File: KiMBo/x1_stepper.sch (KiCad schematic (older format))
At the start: 26 parts

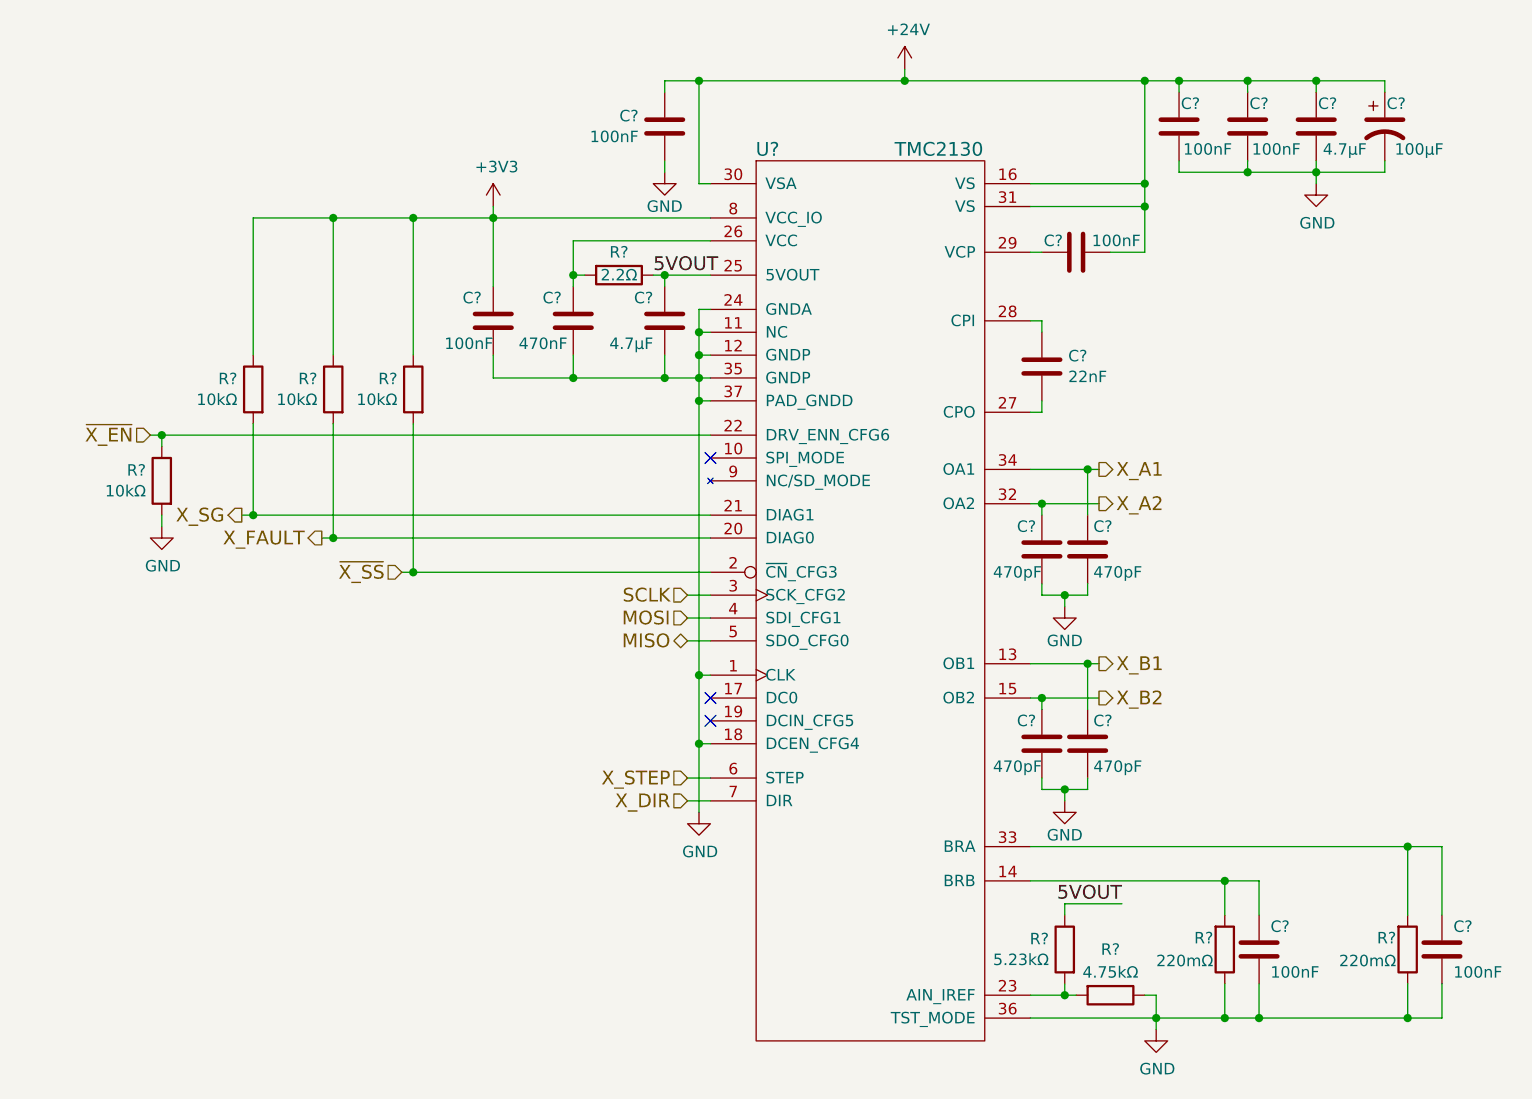
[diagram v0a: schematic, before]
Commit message: Update the rest of the power rails and add two more stepper drivers
Now has *nine* stepper drivers, this will increase cost, and may drastically increase development time...
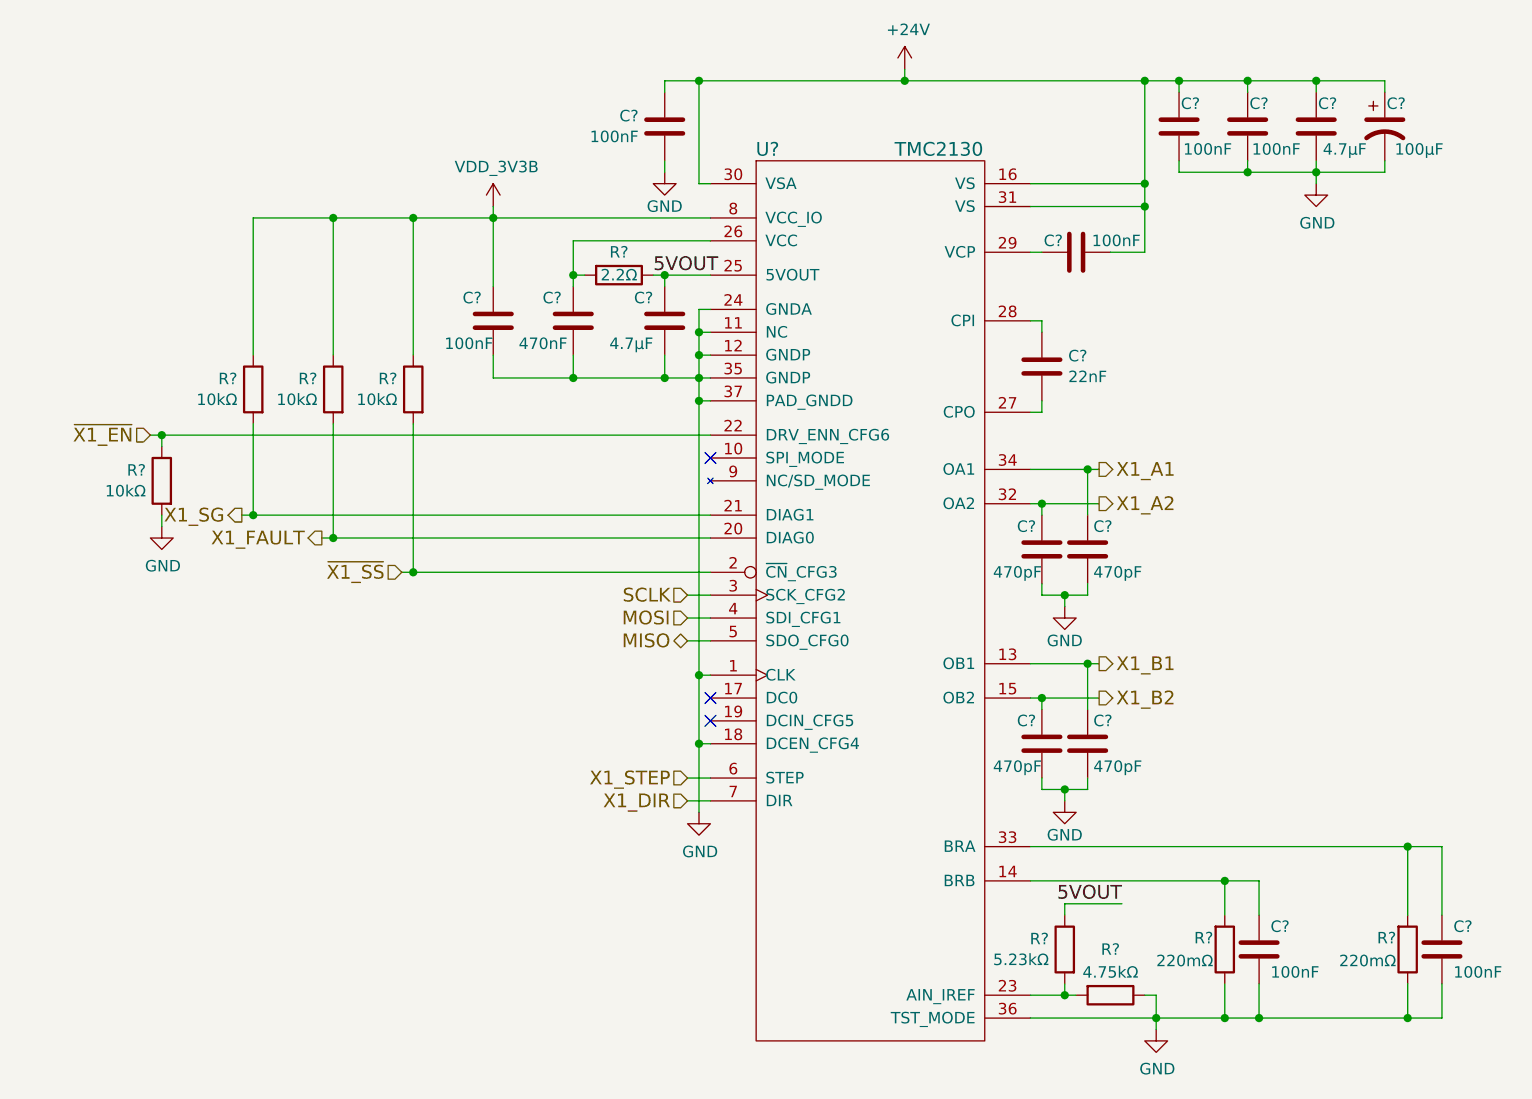
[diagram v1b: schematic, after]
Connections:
- net +3V3 renamed VDD_3V3B
- net X_A1 renamed X1_A1
- net X_A2 renamed X1_A2
- net X_B1 renamed X1_B1
- net X_B2 renamed X1_B2
- net X_DIR renamed X1_DIR
- net X_FAULT renamed X1_FAULT
- net X_SG renamed X1_SG
- net X_STEP renamed X1_STEP
- net ~X_EN renamed ~X1_EN
- net ~X_SS renamed ~X1_SS
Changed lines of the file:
@@
 $Descr A3 16535 11693
 encoding utf-8
-Sheet 13 25
+Sheet 27 27
 Title ""
 Date ""
@@
 $EndDescr
 Text HLabel 9400 4600 2    60   Output ~ 0
-X_A1
+X1_A1
 Text HLabel 9400 4750 2    60   Output ~ 0
-X_A2
+X1_A2
 Text HLabel 9400 5450 2    60   Output ~ 0
-X_B1
+X1_B1
 Text HLabel 9400 5600 2    60   Output ~ 0
-X_B2
+X1_B2
 Text HLabel 7600 5950 0    60   Input ~ 0
-X_STEP
+X1_STEP
 Text HLabel 7600 6050 0    60   Input ~ 0
-X_DIR
+X1_DIR
 Text HLabel 6350 5050 0    60   Input ~ 0
-~X_SS
+~X1_SS
 Text HLabel 7600 5150 0    60   Input ~ 0
 SCLK
@@
 MOSI
 Text HLabel 5650 4800 0    60   Output ~ 0
-X_SG
+X1_SG
 $Comp
 L C C?
@@
 	-1   0    0    -1
 $EndComp
-$Comp
-L +3V3 #PWR?
-U 1 1 58C0931C
-P 6750 3450
-F 0 "#PWR?" H 6750 3300 50  0001 C CNN
-F 1 "+3V3" H 6765 3623 50  0000 C CNN
-F 2 "" H 6750 3450 50  0000 C CNN
-F 3 "" H 6750 3450 50  0000 C CNN
-	1    6750 3450
-	1    0    0    -1
-$EndComp
 NoConn ~ 7700 5700
 $Comp
@@
 $EndComp
 Text HLabel 6000 4900 0    60   Output ~ 0
-X_FAULT
+X1_FAULT
 $Comp
 L R R?
@@
 $EndComp
 Text HLabel 5250 4450 0    60   Input ~ 0
-~X_EN
+~X1_EN
 NoConn ~ 7700 4550
 $Comp
@@
 Wire Wire Line
 	5300 4450 5300 4500
+$Comp
+L VDD_3V3B #PWR?
+U 1 1 5A2FF856
+P 6750 3450
+F 0 "#PWR?" H 6750 3300 50  0001 C CNN
+F 1 "VDD_3V3B" H 6765 3623 50  0000 C CNN
+F 2 "" H 6750 3450 50  0000 C CNN
+F 3 "" H 6750 3450 50  0000 C CNN
+	1    6750 3450
+	1    0    0    -1
+$EndComp
 $EndSCHEMATC

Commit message: Use only one driver on Y, NAND X and Z FAULT and SG signals
Dual X carriage will need to be tested to determine if two seperate drivers are required for X
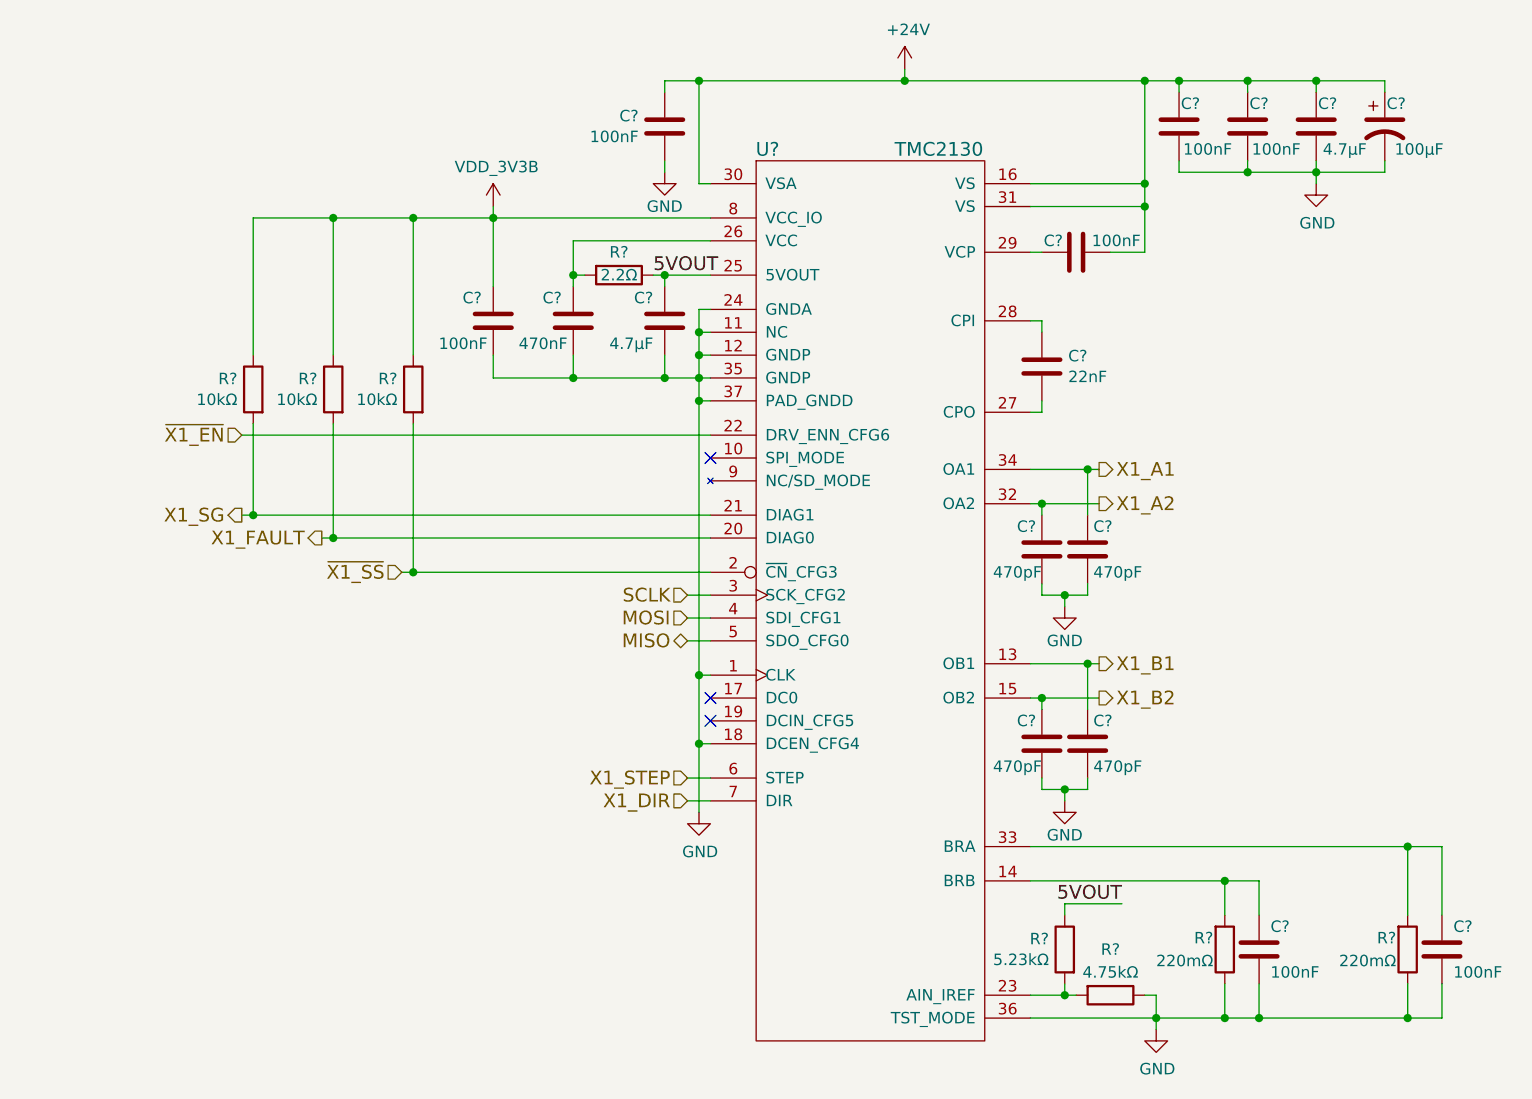
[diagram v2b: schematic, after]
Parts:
- removed C?: 100nF, symbol C
- removed R?: 10kΩ, symbol R
- added C?: 100nF, symbol C
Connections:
- net GND: now also C?.2
- net VDD_3V3B: now also C?.1
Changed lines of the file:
@@
 $Descr A3 16535 11693
 encoding utf-8
-Sheet 27 27
+Sheet 27 26
 Title ""
 Date ""
@@
 	-1   0    0    -1
 $EndComp
-$Comp
-L C C?
-U 1 1 58C09315
-P 6750 3950
-F 0 "C?" H 6800 4050 50  0000 L CNN
-F 1 "100nF" H 6750 3850 50  0000 L CNN
-F 2 "" H 6788 3800 50  0000 C CNN
-F 3 "" H 6750 3950 50  0000 C CNN
-	1    6750 3950
-	-1   0    0    -1
-$EndComp
 NoConn ~ 7700 5700
 $Comp
@@
 	-1   0    0    -1
 $EndComp
-Text HLabel 5250 4450 0    60   Input ~ 0
+Text HLabel 5650 4450 0    60   Input ~ 0
 ~X1_EN
 NoConn ~ 7700 4550
@@
 Connection ~ 7650 4200
 Wire Wire Line
-	6750 4200 7700 4200
+	6750 4200 7100 4200
+Wire Wire Line
+	7100 4200 7500 4200
+Wire Wire Line
+	7500 4200 7650 4200
+Wire Wire Line
+	7650 4200 7700 4200
 Wire Wire Line
 	7650 4300 7700 4300
@@
 Connection ~ 7650 4100
 Wire Wire Line
-	7650 3900 7650 6100
+	7650 3900 7650 4000
+Wire Wire Line
+	7650 4000 7650 4100
+Wire Wire Line
+	7650 4100 7650 4200
+Wire Wire Line
+	7650 4200 7650 4300
+Wire Wire Line
+	7650 4300 7650 5500
+Wire Wire Line
+	7650 5500 7650 5800
+Wire Wire Line
+	7650 5800 7650 6100
 Wire Wire Line
 	7700 3900 7650 3900
@@
 	7650 5500 7700 5500
 Wire Wire Line
-	9100 6250 10900 6250
-Wire Wire Line
-	9100 5600 9400 5600
+	9100 6250 10750 6250
+Wire Wire Line
+	10750 6250 10900 6250
+Wire Wire Line
+	9100 5600 9150 5600
+Wire Wire Line
+	9150 5600 9400 5600
 Wire Wire Line
 	9150 3950 9100 3950
@@
 	10650 3300 10650 3250
 Wire Wire Line
-	9750 3300 10650 3300
+	9750 3300 10050 3300
+Wire Wire Line
+	10050 3300 10350 3300
+Wire Wire Line
+	10350 3300 10650 3300
 Wire Wire Line
 	9750 3250 9750 3300
@@
 	7500 3250 7500 3300
 Wire Wire Line
-	9600 2900 9600 3650
+	9600 2900 9600 3350
+Wire Wire Line
+	9600 3350 9600 3450
+Wire Wire Line
+	9600 3450 9600 3650
 Wire Wire Line
 	9600 3650 9450 3650
@@
 	9100 3650 9150 3650
 Wire Wire Line
-	7500 2900 10650 2900
+	7500 2900 7650 2900
+Wire Wire Line
+	7650 2900 8550 2900
+Wire Wire Line
+	8550 2900 9600 2900
+Wire Wire Line
+	9600 2900 9750 2900
+Wire Wire Line
+	9750 2900 10050 2900
+Wire Wire Line
+	10050 2900 10350 2900
+Wire Wire Line
+	10350 2900 10650 2900
 Wire Wire Line
 	7650 3350 7650 2900
 Wire Wire Line
-	7450 3750 7700 3750
+	7450 3750 7500 3750
+Wire Wire Line
+	7500 3750 7700 3750
 Wire Wire Line
 	7700 4100 7650 4100
@@
 	7100 4100 7100 4200
 Wire Wire Line
-	7100 3600 7100 3800
+	7100 3600 7100 3750
+Wire Wire Line
+	7100 3750 7100 3800
 Wire Wire Line
 	7100 3750 7150 3750
@@
 Connection ~ 7100 3750
 Wire Wire Line
-	6750 3450 6750 3800
+	6750 3450 6750 3500
+Wire Wire Line
+	6750 3500 6750 3800
 Wire Wire Line
 	6750 4100 6750 4200
@@
 Connection ~ 10750 7000
 Wire Wire Line
-	9100 6400 10100 6400
+	9100 6400 9950 6400
+Wire Wire Line
+	9950 6400 10100 6400
 Connection ~ 10750 6250
 Wire Wire Line
-	6000 4900 7700 4900
+	6000 4900 6050 4900
+Wire Wire Line
+	6050 4900 7700 4900
 Wire Wire Line
 	6050 4400 6050 4900
@@
 Connection ~ 6050 4900
 Wire Wire Line
-	5250 4450 7700 4450
+	5650 4450 7700 4450
 Wire Wire Line
 	7500 3800 7500 3750
 Wire Wire Line
-	9100 6900 9300 6900
+	9100 6900 9250 6900
+Wire Wire Line
+	9250 6900 9300 6900
 Wire Wire Line
 	9250 6550 9250 6500
@@
 Connection ~ 9250 6900
 Wire Wire Line
-	9650 6900 9650 7050
+	9650 6900 9650 7000
+Wire Wire Line
+	9650 7000 9650 7050
 Connection ~ 9650 7000
 Wire Wire Line
 	9650 6900 9600 6900
 Wire Wire Line
-	6350 5050 7700 5050
+	6350 5050 6400 5050
+Wire Wire Line
+	6400 5050 7700 5050
 Wire Wire Line
 	6400 5050 6400 4400
@@
 Connection ~ 6400 3500
 Wire Wire Line
-	5650 4800 7700 4800
-Wire Wire Line
-	9150 5150 9350 5150
+	5650 4800 5700 4800
+Wire Wire Line
+	5700 4800 7700 4800
+Wire Wire Line
+	9150 5150 9250 5150
+Wire Wire Line
+	9250 5150 9350 5150
 Wire Wire Line
 	9150 4750 9150 4800
 Connection ~ 9150 4750
 Wire Wire Line
-	9150 6000 9350 6000
+	9150 6000 9250 6000
+Wire Wire Line
+	9250 6000 9350 6000
 Wire Wire Line
 	9150 5600 9150 5650
 Connection ~ 9150 5600
 Wire Wire Line
-	9100 7000 10900 7000
+	9100 7000 9650 7000
+Wire Wire Line
+	9650 7000 9950 7000
+Wire Wire Line
+	9950 7000 10100 7000
+Wire Wire Line
+	10100 7000 10750 7000
+Wire Wire Line
+	10750 7000 10900 7000
 Wire Wire Line
 	9250 6500 9500 6500
@@
 Connection ~ 10350 2900
 Wire Wire Line
-	10350 3250 10350 3350
+	10350 3250 10350 3300
+Wire Wire Line
+	10350 3300 10350 3350
 Connection ~ 10350 3300
 Wire Wire Line
 	10050 3250 10050 3300
 Wire Wire Line
-	9100 5450 9400 5450
+	9100 5450 9350 5450
+Wire Wire Line
+	9350 5450 9400 5450
 Wire Wire Line
 	9350 6000 9350 5950
@@
 	9350 5150 9350 5100
 Wire Wire Line
-	9100 4750 9400 4750
-Wire Wire Line
-	9100 4600 9400 4600
-$Comp
-L R R?
-U 1 1 58C09421
-P 5300 4650
-F 0 "R?" H 5369 4696 50  0000 L CNN
-F 1 "10kΩ" H 5369 4605 50  0000 L CNN
-F 2 "" V 5230 4650 50  0000 C CNN
-F 3 "" H 5300 4650 50  0000 C CNN
-	1    5300 4650
-	-1   0    0    -1
-$EndComp
-Connection ~ 5300 4450
-Wire Wire Line
-	5700 3500 7700 3500
-$Comp
-L GND #PWR?
-U 1 1 58C0942B
-P 5300 4850
-F 0 "#PWR?" H 5300 4600 50  0001 C CNN
-F 1 "GND" H 5305 4677 50  0000 C CNN
-F 2 "" H 5300 4850 50  0000 C CNN
-F 3 "" H 5300 4850 50  0000 C CNN
-	1    5300 4850
-	1    0    0    -1
-$EndComp
-Wire Wire Line
-	5300 4850 5300 4800
-Wire Wire Line
-	5300 4450 5300 4500
+	9100 4750 9150 4750
+Wire Wire Line
+	9150 4750 9400 4750
+Wire Wire Line
+	9100 4600 9350 4600
+Wire Wire Line
+	9350 4600 9400 4600
+Wire Wire Line
+	5700 3500 6050 3500
+Wire Wire Line
+	6050 3500 6400 3500
+Wire Wire Line
+	6400 3500 6750 3500
+Wire Wire Line
+	6750 3500 7700 3500
 $Comp
 L VDD_3V3B #PWR?
@@
 	1    0    0    -1
 $EndComp
+$Comp
+L C C?
+U 1 1 5A89A0A1
+P 6750 3950
+F 0 "C?" H 6800 4050 50  0000 L CNN
+F 1 "100nF" H 6775 3850 50  0000 L CNN
+F 2 "" H 6788 3800 50  0000 C CNN
+F 3 "" H 6750 3950 50  0000 C CNN
+	1    6750 3950
+	-1   0    0    -1
+$EndComp
 $EndSCHEMATC

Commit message: Annotate all components, now passing ERC, added ferrites to the rest of the connectors
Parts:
- removed C?: 100μF, symbol CP1
- removed C? (x2): 100nF, symbol C
- removed C?: 22nF, symbol C
- removed C? (x3): 470pF, symbol C
- removed R? (x2): 220mΩ, symbol R
- removed R? (x2): 10kΩ, symbol R
- removed U?: TMC2130, symbol TMC2130
- added C201: 22nF, symbol C
- added C202, C205, C206: 470pF, symbol C
- added C207, C212: 100nF, symbol C
- added C211: 100μF, symbol CP1
- added R189, R190: 10kΩ, symbol R
- added R194, R195: 220mΩ, symbol R
- added U28: TMC2130, symbol TMC2130
- gave numbers to parts that had none: 13
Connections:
- net +24V: now also C207.1, C211.1, U28.16 (VS), U28.30 (VSA), U28.31 (VS)
- net 5VOUT: now also U28.25 (5VOUT)
- net GND: now also C202.2, C205.2, C206.2, C207.2, C211.2, C212.2, R194.1, R195.1, U28.1 (CLK), U28.11 (NC), U28.12 (GNDP), U28.18 (DCEN_CFG4), U28.24 (GNDA), U28.35 (GNDP), U28.36 (TST_MODE), U28.37 (PAD_GNDD)
- net MISO: now also U28.5 (SDO_CFG0)
- net MOSI: now also U28.4 (SDI_CFG1)
- net SCLK: now also U28.3 (SCK_CFG2)
- net VDD_3V3B: now also R189.1, R190.1, U28.8 (VCC_IO)
- net X1_A1: now also C205.1, U28.34 (OA1)
- net X1_A2: now also C202.1, U28.32 (OA2)
- net X1_B1: now also C206.1, U28.13 (OB1)
- net X1_B2: now also U28.15 (OB2)
- net X1_DIR: now also U28.7 (DIR)
- net X1_FAULT: now also R189.2, U28.20 (DIAG0)
- net X1_SG: now also U28.21 (DIAG1)
- net X1_STEP: now also U28.6 (STEP)
- net ~X1_EN: now also U28.22 (DRV_ENN_CFG6)
- net ~X1_SS: now also R190.2, U28.2 (~CN~_CFG3)
- net at C204.2: now also U28.29 (VCP)
- net at C209.1: now also R194.2, U28.14 (BRB)
- net at C198.1, R191.2: now also U28.26 (VCC)
- net at R192.2, R193.2: now also U28.23 (AIN_IREF)
- new net: C201.1, U28.28 (CPI)
- new net: C201.2, U28.27 (CPO)
- new net: C212.1, R195.2, U28.33 (BRA)
